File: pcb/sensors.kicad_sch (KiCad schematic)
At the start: 21 parts, among them J4 Conn_01x04, J5 Conn_01x04, J6 6P4C, J7 Conn_02x05_Odd_Even, U10 TXS0108EPW, U11 BME280, U12 SGP41, U9 SN65HVD3082EDR

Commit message: chore: re-annotate
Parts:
- renumbered R16 to R17, R17 to R18, R18 to R19, R19 to R20, R20 to R21, R21 to R22
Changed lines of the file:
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@@
 		(on_board yes)
 		(dnp no)
-		(property "Reference" "R20"
+		(property "Reference" "R21"
 			(at 41.91 157.4799 0)
 			(effects
@@
 			(project ""
 				(path "/9bba97c2-2e09-46fb-bf2a-7de104403c7c/0b6630c6-ecdb-4ee5-ae06-53316b49d000"
-					(reference "R20")
+					(reference "R21")
 					(unit 1)
 				)
@@
 		(dnp no)
 		(fields_autoplaced yes)
-		(property "Reference" "#PWR070"
+		(property "Reference" "#PWR071"
 			(at 88.9 161.29 0)
 			(effects
@@
 			(project ""
 				(path "/9bba97c2-2e09-46fb-bf2a-7de104403c7c/0b6630c6-ecdb-4ee5-ae06-53316b49d000"
-					(reference "#PWR070")
+					(reference "#PWR071")
 					(unit 1)
 				)
@@
 		(dnp no)
 		(fields_autoplaced yes)
-		(property "Reference" "#PWR072"
+		(property "Reference" "#PWR073"
 			(at 73.66 160.02 0)
 			(effects
@@
 			(project "pcb"
 				(path "/9bba97c2-2e09-46fb-bf2a-7de104403c7c/0b6630c6-ecdb-4ee5-ae06-53316b49d000"
-					(reference "#PWR072")
+					(reference "#PWR073")
 					(unit 1)
 				)
@@
 		(on_board yes)
 		(dnp no)
-		(property "Reference" "R16"
+		(property "Reference" "R17"
 			(at 242.57 48.2599 0)
 			(effects
@@
 			(project "pcb"
 				(path "/9bba97c2-2e09-46fb-bf2a-7de104403c7c/0b6630c6-ecdb-4ee5-ae06-53316b49d000"
-					(reference "R16")
+					(reference "R17")
 					(unit 1)
 				)
@@
 		(dnp no)
 		(fields_autoplaced yes)
-		(property "Reference" "#PWR073"
+		(property "Reference" "#PWR074"
 			(at 50.8 162.56 0)
 			(effects
@@
 			(project ""
 				(path "/9bba97c2-2e09-46fb-bf2a-7de104403c7c/0b6630c6-ecdb-4ee5-ae06-53316b49d000"
-					(reference "#PWR073")
+					(reference "#PWR074")
 					(unit 1)
 				)
@@
 		(dnp no)
 		(fields_autoplaced yes)
-		(property "Reference" "#PWR074"
+		(property "Reference" "#PWR075"
 			(at 83.82 162.56 0)
 			(effects
@@
 			(project ""
 				(path "/9bba97c2-2e09-46fb-bf2a-7de104403c7c/0b6630c6-ecdb-4ee5-ae06-53316b49d000"
-					(reference "#PWR074")
+					(reference "#PWR075")
 					(unit 1)
 				)
@@
 		(dnp no)
 		(fields_autoplaced yes)
-		(property "Reference" "#PWR067"
+		(property "Reference" "#PWR068"
 			(at 186.69 125.73 0)
 			(effects
@@
 			(project ""
 				(path "/9bba97c2-2e09-46fb-bf2a-7de104403c7c/0b6630c6-ecdb-4ee5-ae06-53316b49d000"
-					(reference "#PWR067")
+					(reference "#PWR068")
 					(unit 1)
 				)
@@
 		(dnp no)
 		(fields_autoplaced yes)
-		(property "Reference" "#PWR056"
+		(property "Reference" "#PWR057"
 			(at 160.02 35.56 0)
 			(effects
@@
 			(project "pcb"
 				(path "/9bba97c2-2e09-46fb-bf2a-7de104403c7c/0b6630c6-ecdb-4ee5-ae06-53316b49d000"
-					(reference "#PWR056")
+					(reference "#PWR057")
 					(unit 1)
 				)
@@
 		(dnp no)
 		(fields_autoplaced yes)
-		(property "Reference" "#PWR058"
+		(property "Reference" "#PWR059"
 			(at 35.56 48.26 0)
 			(effects
@@
 			(project "pcb"
 				(path "/9bba97c2-2e09-46fb-bf2a-7de104403c7c/0b6630c6-ecdb-4ee5-ae06-53316b49d000"
-					(reference "#PWR058")
+					(reference "#PWR059")
 					(unit 1)
 				)
@@
 		(dnp no)
 		(fields_autoplaced yes)
-		(property "Reference" "R18"
+		(property "Reference" "R19"
 			(at 46.99 102.8699 0)
 			(effects
@@
 			(project ""
 				(path "/9bba97c2-2e09-46fb-bf2a-7de104403c7c/0b6630c6-ecdb-4ee5-ae06-53316b49d000"
-					(reference "R18")
+					(reference "R19")
 					(unit 1)
 				)
@@
 		(dnp no)
 		(fields_autoplaced yes)
-		(property "Reference" "#PWR064"
+		(property "Reference" "#PWR065"
 			(at 190.5 100.33 0)
 			(effects
@@
 			(project ""
 				(path "/9bba97c2-2e09-46fb-bf2a-7de104403c7c/0b6630c6-ecdb-4ee5-ae06-53316b49d000"
-					(reference "#PWR064")
+					(reference "#PWR065")
 					(unit 1)
 				)
@@
 		(dnp no)
 		(fields_autoplaced yes)
-		(property "Reference" "#PWR054"
+		(property "Reference" "#PWR055"
 			(at 247.65 29.21 0)
 			(effects
@@
 			(project "pcb"
 				(path "/9bba97c2-2e09-46fb-bf2a-7de104403c7c/0b6630c6-ecdb-4ee5-ae06-53316b49d000"
-					(reference "#PWR054")
+					(reference "#PWR055")
 					(unit 1)
 				)
@@
 		(dnp no)
 		(fields_autoplaced yes)
-		(property "Reference" "#PWR053"
+		(property "Reference" "#PWR054"
 			(at 193.04 29.21 0)
 			(effects
@@
 			(project "pcb"
 				(path "/9bba97c2-2e09-46fb-bf2a-7de104403c7c/0b6630c6-ecdb-4ee5-ae06-53316b49d000"
-					(reference "#PWR053")
+					(reference "#PWR054")
 					(unit 1)
 				)
@@
 		(dnp no)
 		(fields_autoplaced yes)
-		(property "Reference" "#PWR069"
+		(property "Reference" "#PWR070"
 			(at 44.45 156.21 0)
 			(effects
@@
 			(project ""
 				(path "/9bba97c2-2e09-46fb-bf2a-7de104403c7c/0b6630c6-ecdb-4ee5-ae06-53316b49d000"
-					(reference "#PWR069")
+					(reference "#PWR070")
 					(unit 1)
 				)
@@
 		(dnp no)
 		(fields_autoplaced yes)
-		(property "Reference" "#PWR057"
+		(property "Reference" "#PWR058"
 			(at 218.44 35.56 0)
 			(effects
@@
 			(project "pcb"
 				(path "/9bba97c2-2e09-46fb-bf2a-7de104403c7c/0b6630c6-ecdb-4ee5-ae06-53316b49d000"
-					(reference "#PWR057")
+					(reference "#PWR058")
 					(unit 1)
 				)
@@
 		(dnp no)
 		(fields_autoplaced yes)
-		(property "Reference" "#PWR068"
+		(property "Reference" "#PWR069"
 			(at 44.45 138.43 0)
 			(effects
@@
 			(project ""
 				(path "/9bba97c2-2e09-46fb-bf2a-7de104403c7c/0b6630c6-ecdb-4ee5-ae06-53316b49d000"
-					(reference "#PWR068")
+					(reference "#PWR069")
 					(unit 1)
 				)
@@
 		(dnp no)
 		(fields_autoplaced yes)
-		(property "Reference" "#PWR066"
+		(property "Reference" "#PWR067"
 			(at 250.19 111.76 0)
 			(effects
@@
 			(project ""
 				(path "/9bba97c2-2e09-46fb-bf2a-7de104403c7c/0b6630c6-ecdb-4ee5-ae06-53316b49d000"
-					(reference "#PWR066")
+					(reference "#PWR067")
 					(unit 1)
 				)
@@
 		(dnp no)
 		(fields_autoplaced yes)
-		(property "Reference" "#PWR065"
+		(property "Reference" "#PWR066"
 			(at 41.91 101.6 0)
 			(effects
@@
 			(project ""
 				(path "/9bba97c2-2e09-46fb-bf2a-7de104403c7c/0b6630c6-ecdb-4ee5-ae06-53316b49d000"
-					(reference "#PWR065")
+					(reference "#PWR066")
 					(unit 1)
 				)
@@
 		(dnp no)
 		(fields_autoplaced yes)
-		(property "Reference" "R17"
+		(property "Reference" "R18"
 			(at 176.53 96.52 90)
 			(effects
@@
 			(project ""
 				(path "/9bba97c2-2e09-46fb-bf2a-7de104403c7c/0b6630c6-ecdb-4ee5-ae06-53316b49d000"
-					(reference "R17")
+					(reference "R18")
 					(unit 1)
 				)
@@
 		(dnp no)
 		(fields_autoplaced yes)
-		(property "Reference" "#PWR071"
+		(property "Reference" "#PWR072"
 			(at 60.96 160.02 0)
 			(effects
@@
 			(project ""
 				(path "/9bba97c2-2e09-46fb-bf2a-7de104403c7c/0b6630c6-ecdb-4ee5-ae06-53316b49d000"
-					(reference "#PWR071")
+					(reference "#PWR072")
 					(unit 1)
 				)
@@
 		(dnp no)
 		(fields_autoplaced yes)
-		(property "Reference" "#PWR061"
+		(property "Reference" "#PWR062"
 			(at 190.5 74.93 0)
 			(effects
@@
 			(project "pcb"
 				(path "/9bba97c2-2e09-46fb-bf2a-7de104403c7c/0b6630c6-ecdb-4ee5-ae06-53316b49d000"
-					(reference "#PWR061")
+					(reference "#PWR062")
 					(unit 1)
 				)
@@
 		(dnp no)
 		(fields_autoplaced yes)
-		(property "Reference" "#PWR063"
+		(property "Reference" "#PWR064"
 			(at 247.65 80.01 0)
 			(effects
@@
 			(project ""
 				(path "/9bba97c2-2e09-46fb-bf2a-7de104403c7c/0b6630c6-ecdb-4ee5-ae06-53316b49d000"
-					(reference "#PWR063")
+					(reference "#PWR064")
 					(unit 1)
 				)
@@
 		(dnp no)
 		(fields_autoplaced yes)
-		(property "Reference" "#PWR060"
+		(property "Reference" "#PWR061"
 			(at 247.65 60.96 0)
 			(effects
@@
 			(project "pcb"
 				(path "/9bba97c2-2e09-46fb-bf2a-7de104403c7c/0b6630c6-ecdb-4ee5-ae06-53316b49d000"
-					(reference "#PWR060")
+					(reference "#PWR061")
 					(unit 1)
 				)
@@
 		(dnp no)
 		(fields_autoplaced yes)
-		(property "Reference" "#PWR055"
+		(property "Reference" "#PWR056"
 			(at 29.21 30.48 0)
 			(effects
@@
 			(project ""
 				(path "/9bba97c2-2e09-46fb-bf2a-7de104403c7c/0b6630c6-ecdb-4ee5-ae06-53316b49d000"
-					(reference "#PWR055")
+					(reference "#PWR056")
 					(unit 1)
 				)
@@
 		(dnp no)
 		(fields_autoplaced yes)
-		(property "Reference" "#PWR052"
+		(property "Reference" "#PWR053"
 			(at 187.96 29.21 0)
 			(effects
@@
 			(project "pcb"
 				(path "/9bba97c2-2e09-46fb-bf2a-7de104403c7c/0b6630c6-ecdb-4ee5-ae06-53316b49d000"
-					(reference "#PWR052")
+					(reference "#PWR053")
 					(unit 1)
 				)
@@
 		(dnp no)
 		(fields_autoplaced yes)
-		(property "Reference" "R21"
+		(property "Reference" "R22"
 			(at 91.44 162.5599 0)
 			(effects
@@
 			(project ""
 				(path "/9bba97c2-2e09-46fb-bf2a-7de104403c7c/0b6630c6-ecdb-4ee5-ae06-53316b49d000"
-					(reference "R21")
+					(reference "R22")
 					(unit 1)
 				)
@@
 		(dnp no)
 		(fields_autoplaced yes)
-		(property "Reference" "#PWR062"
+		(property "Reference" "#PWR063"
 			(at 49.53 82.55 0)
 			(effects
@@
 			(project ""
 				(path "/9bba97c2-2e09-46fb-bf2a-7de104403c7c/0b6630c6-ecdb-4ee5-ae06-53316b49d000"
-					(reference "#PWR062")
+					(reference "#PWR063")
 					(unit 1)
 				)
@@
 		(dnp no)
 		(fields_autoplaced yes)
-		(property "Reference" "R19"
+		(property "Reference" "R20"
 			(at 191.77 109.2199 0)
 			(effects
@@
 			(project ""
 				(path "/9bba97c2-2e09-46fb-bf2a-7de104403c7c/0b6630c6-ecdb-4ee5-ae06-53316b49d000"
-					(reference "R19")
+					(reference "R20")
 					(unit 1)
 				)
@@
 		(dnp no)
 		(fields_autoplaced yes)
-		(property "Reference" "#PWR059"
+		(property "Reference" "#PWR060"
 			(at 74.93 45.72 0)
 			(effects
@@
 			(project ""
 				(path "/9bba97c2-2e09-46fb-bf2a-7de104403c7c/0b6630c6-ecdb-4ee5-ae06-53316b49d000"
-					(reference "#PWR059")
+					(reference "#PWR060")
 					(unit 1)
 				)

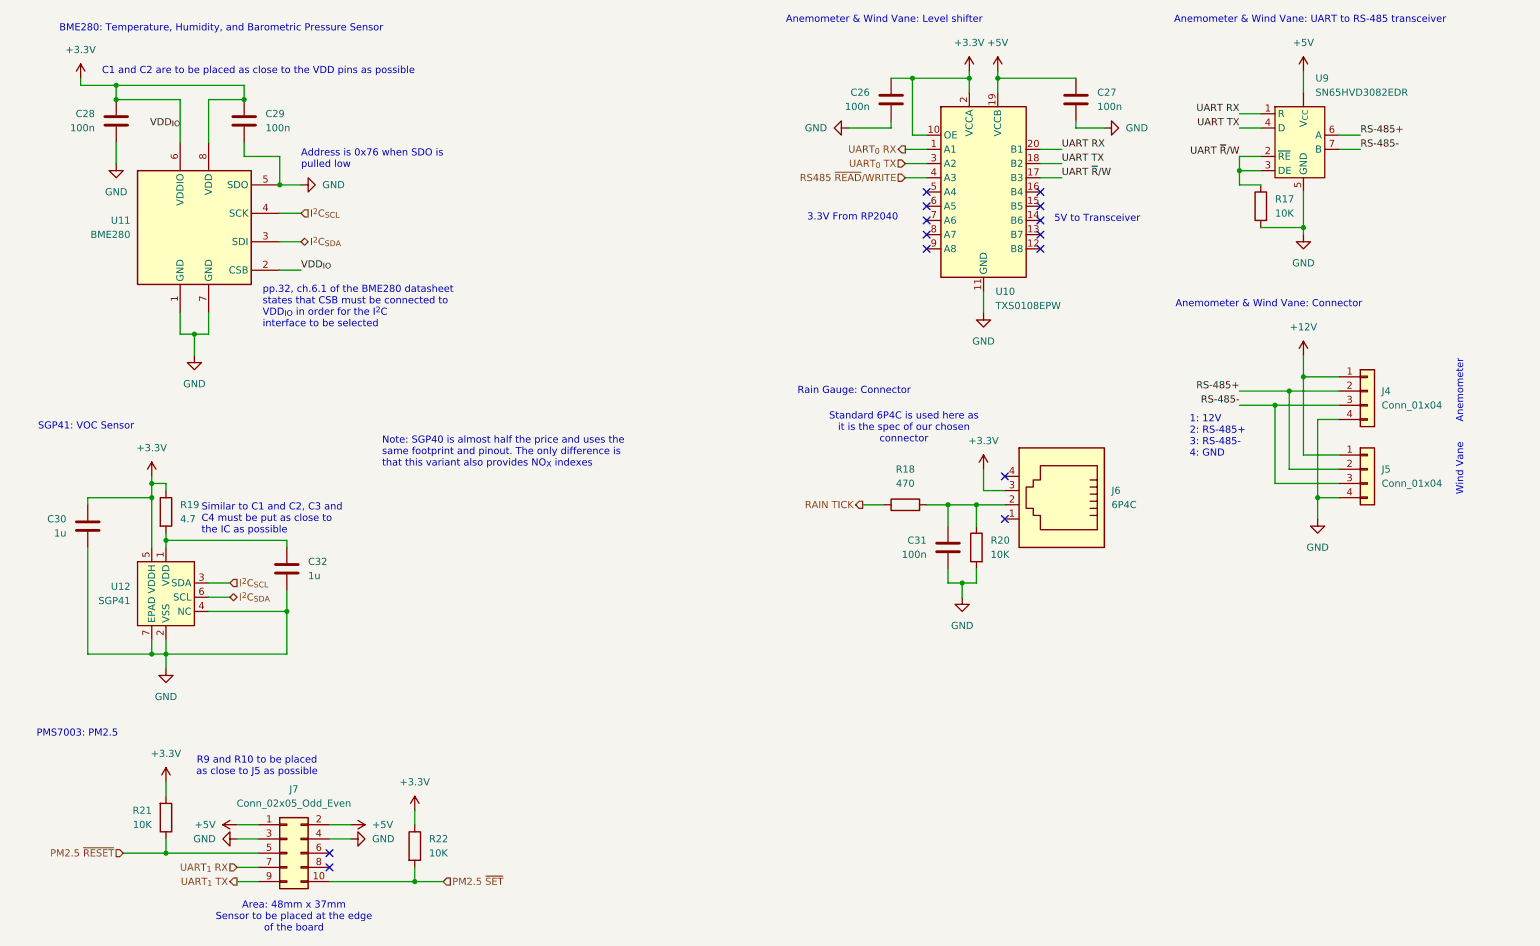
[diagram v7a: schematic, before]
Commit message: feat: changed 5v boost controller
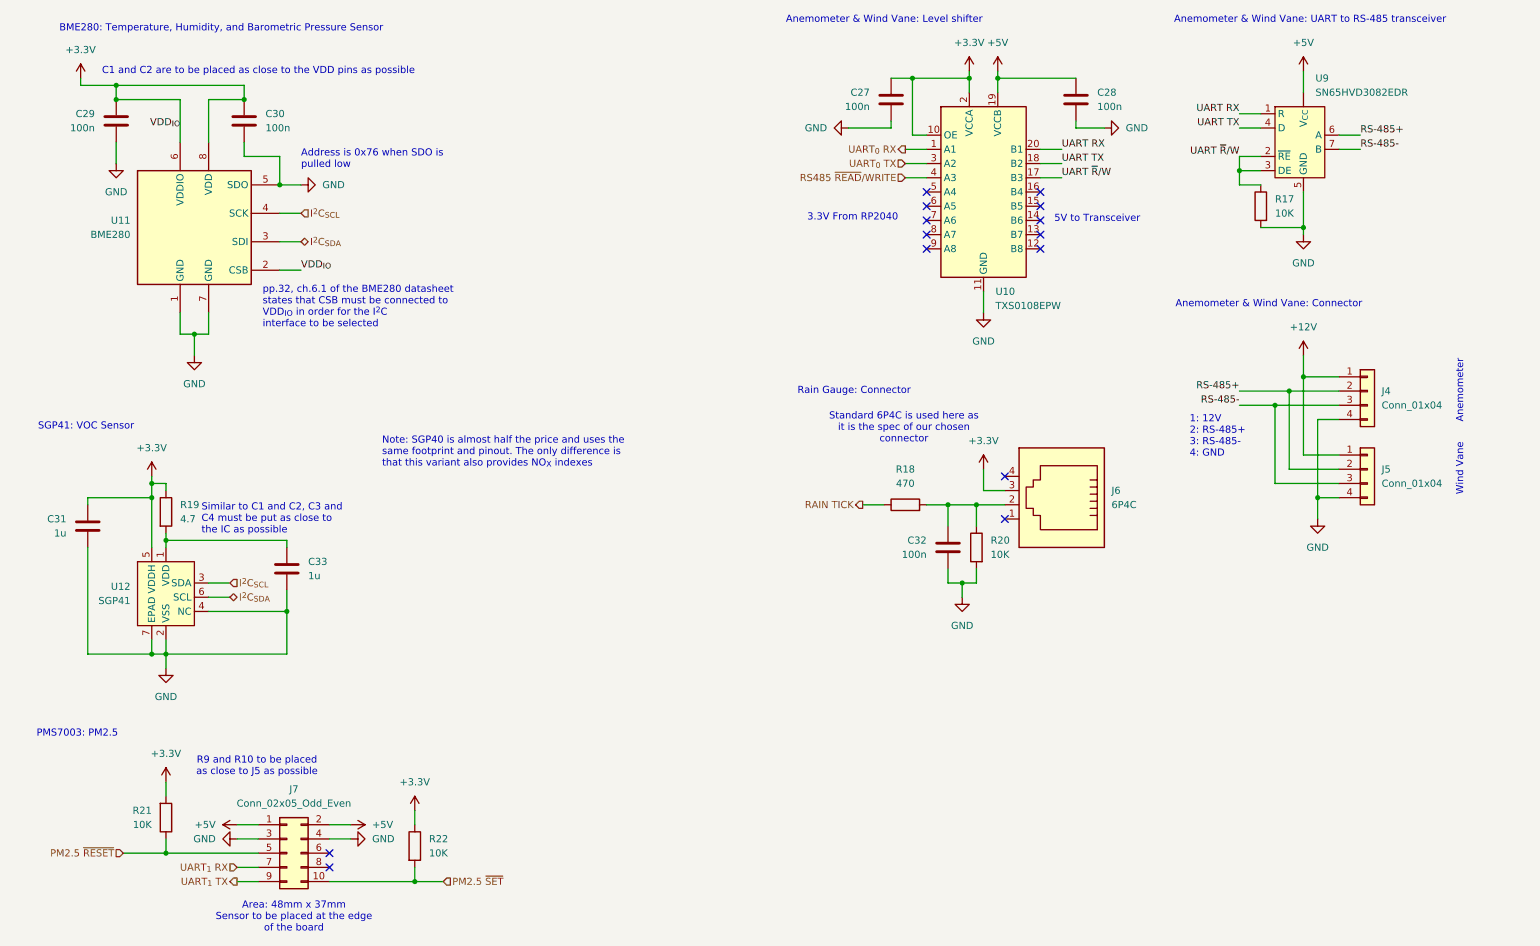
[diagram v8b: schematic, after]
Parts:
- renumbered C26 to C27, C27 to C28, C28 to C29, C29 to C30, C30 to C31, C31 to C32, C32 to C33
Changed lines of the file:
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@@
 		(dnp no)
 		(fields_autoplaced yes)
-		(property "Reference" "C29"
+		(property "Reference" "C30"
 			(at 62.23 33.0199 0)
 			(effects
@@
 			(project ""
 				(path "/9bba97c2-2e09-46fb-bf2a-7de104403c7c/0b6630c6-ecdb-4ee5-ae06-53316b49d000"
-					(reference "C29")
+					(reference "C30")
 					(unit 1)
 				)
@@
 		(on_board yes)
 		(dnp no)
-		(property "Reference" "C28"
+		(property "Reference" "C29"
 			(at 31.75 33.0199 0)
 			(effects
@@
 			(project ""
 				(path "/9bba97c2-2e09-46fb-bf2a-7de104403c7c/0b6630c6-ecdb-4ee5-ae06-53316b49d000"
-					(reference "C28")
+					(reference "C29")
 					(unit 1)
 				)
@@
 		(dnp no)
 		(fields_autoplaced yes)
-		(property "Reference" "C32"
+		(property "Reference" "C33"
 			(at 69.85 113.0299 0)
 			(effects
@@
 			(project ""
 				(path "/9bba97c2-2e09-46fb-bf2a-7de104403c7c/0b6630c6-ecdb-4ee5-ae06-53316b49d000"
-					(reference "C32")
+					(reference "C33")
 					(unit 1)
 				)
@@
 		(on_board yes)
 		(dnp no)
-		(property "Reference" "C27"
+		(property "Reference" "C28"
 			(at 210.82 29.2099 0)
 			(effects
@@
 			(project "pcb"
 				(path "/9bba97c2-2e09-46fb-bf2a-7de104403c7c/0b6630c6-ecdb-4ee5-ae06-53316b49d000"
-					(reference "C27")
+					(reference "C28")
 					(unit 1)
 				)
@@
 		(on_board yes)
 		(dnp no)
-		(property "Reference" "C30"
+		(property "Reference" "C31"
 			(at 26.67 105.4099 0)
 			(effects
@@
 			(project ""
 				(path "/9bba97c2-2e09-46fb-bf2a-7de104403c7c/0b6630c6-ecdb-4ee5-ae06-53316b49d000"
-					(reference "C30")
+					(reference "C31")
 					(unit 1)
 				)
@@
 		(dnp no)
 		(fields_autoplaced yes)
-		(property "Reference" "C26"
+		(property "Reference" "C27"
 			(at 170.18 29.2099 0)
 			(effects
@@
 			(project "pcb"
 				(path "/9bba97c2-2e09-46fb-bf2a-7de104403c7c/0b6630c6-ecdb-4ee5-ae06-53316b49d000"
-					(reference "C26")
+					(reference "C27")
 					(unit 1)
 				)
@@
 		(on_board yes)
 		(dnp no)
-		(property "Reference" "C31"
+		(property "Reference" "C32"
 			(at 180.34 109.2199 0)
 			(effects
@@
 			(project ""
 				(path "/9bba97c2-2e09-46fb-bf2a-7de104403c7c/0b6630c6-ecdb-4ee5-ae06-53316b49d000"
-					(reference "C31")
-					(unit 1)
-				)
+					(reference "C32")
+					(unit 1)
+				)
